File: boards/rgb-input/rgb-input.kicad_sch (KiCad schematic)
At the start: 22 parts, among them J1 Conn_01x03, J10 Conn_01x03, J11 Conn_01x03, J12 Conn_01x03, J15 Conn_01x03, J16 Conn_01x03, J17 Conn_01x03, J18 Conn_01x03, J2 Conn_01x03, J3 Conn_01x03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

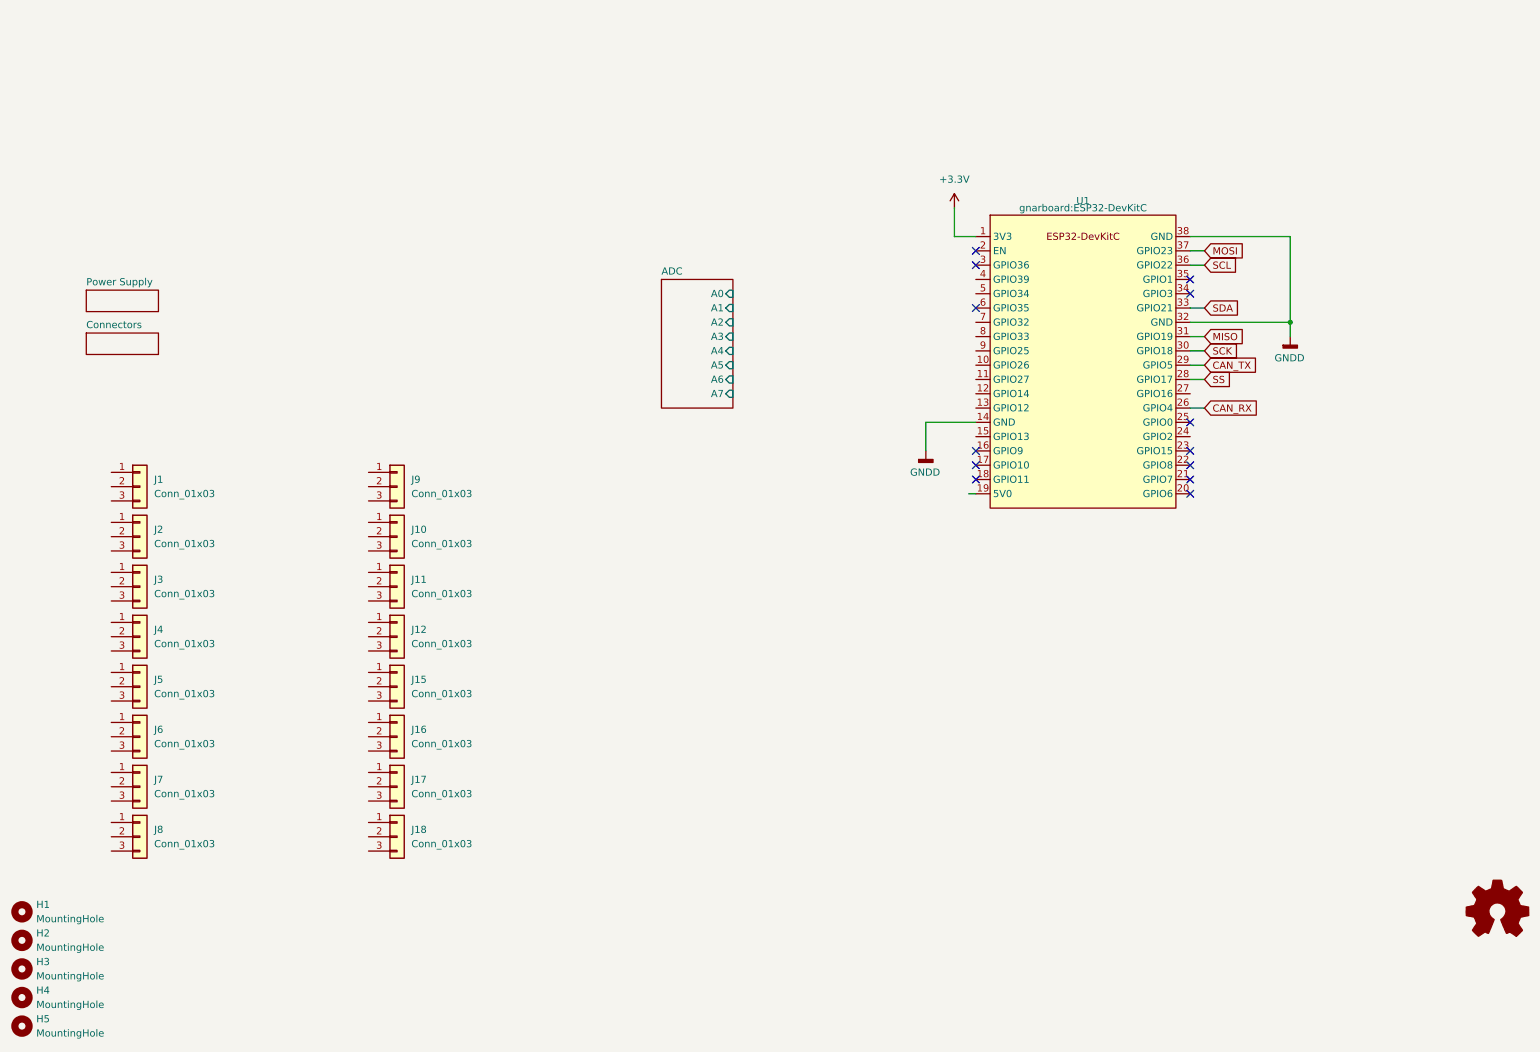
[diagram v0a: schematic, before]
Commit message: input board shaping up to be lit.
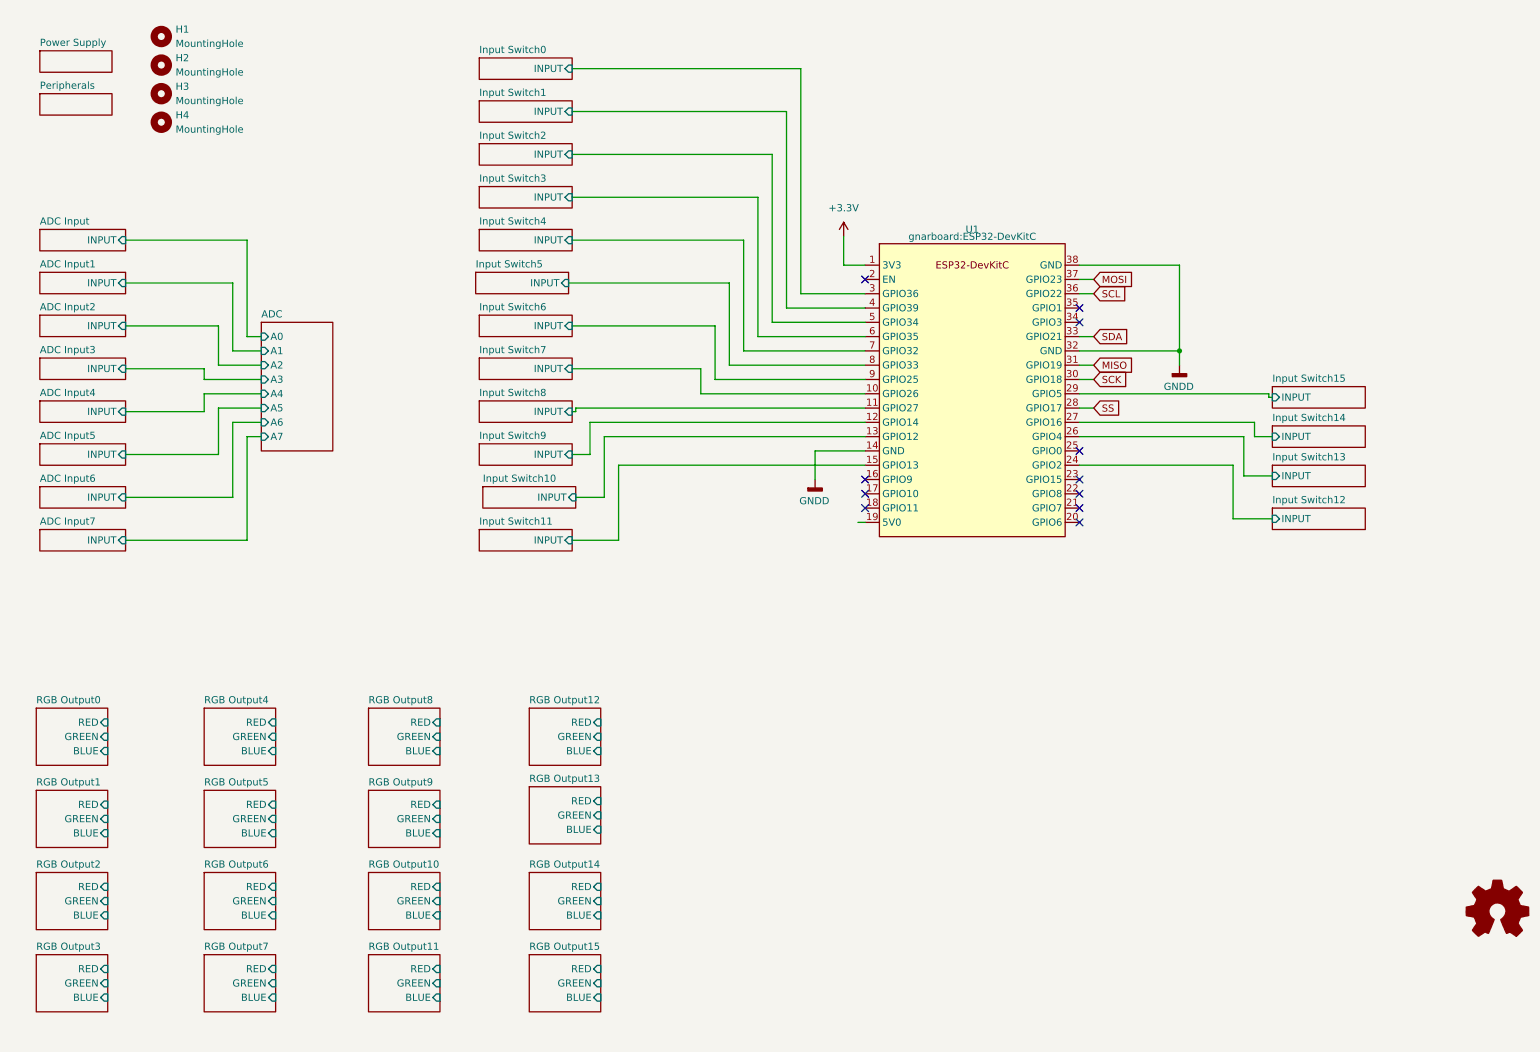
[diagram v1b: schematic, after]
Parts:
- removed H5: MountingHole, MountingHole:MountingHole_3.2mm_M3_DIN965_Pad, symbol Mechanical:MountingHole
- removed J1, J10, J11, J12, J15, J16, J17, J18, J2, J3, J4, J5, J6, J7, J8, J9: Conn_01x03, Connector_JST:JST_PH_B3B-PH-K_1x03_P2.00mm_Vertical, symbol Connector_Generic:Conn_01x03
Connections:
- net Input Switch7/INPUT: now reaches U1.10 (GPIO26)
- net Input Switch8/INPUT: now reaches U1.11 (GPIO27)
- net Input Switch9/INPUT: now reaches U1.12 (GPIO14)
- net Input Switch10/INPUT: now reaches U1.13 (GPIO12)
- net Input Switch11/INPUT: now reaches U1.15 (GPIO13)
- net Input Switch12/INPUT: now reaches U1.24 (GPIO2)
- net Input Switch14/INPUT: now reaches U1.27 (GPIO16)
- net Input Switch0/INPUT: now reaches U1.3 (GPIO36)
- net Input Switch1/INPUT: now reaches U1.4 (GPIO39)
- net Input Switch2/INPUT: now reaches U1.5 (GPIO34)
- net Input Switch3/INPUT: now reaches U1.6 (GPIO35)
- net Input Switch4/INPUT: now reaches U1.7 (GPIO32)
- net Input Switch5/INPUT: now reaches U1.8 (GPIO33)
- net Input Switch6/INPUT: now reaches U1.9 (GPIO25)
- net CAN_RX renamed Input Switch13/INPUT
- net CAN_TX renamed Input Switch15/INPUT
- no-connect marks 13 -> 11
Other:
- sheet Connectors renamed Peripherals
- added sheet ADC Input (adc input.kicad_sch)
- added sheet ADC Input1 (adc input.kicad_sch)
- added sheet ADC Input2 (adc input.kicad_sch)
- added sheet ADC Input3 (adc input.kicad_sch)
- added sheet ADC Input4 (adc input.kicad_sch)
- added sheet ADC Input5 (adc input.kicad_sch)
- added sheet ADC Input6 (adc input.kicad_sch)
- added sheet ADC Input7 (adc input.kicad_sch)
- added sheet Input Switch0 (input switch.kicad_sch)
- added sheet Input Switch1 (input switch.kicad_sch)
- added sheet Input Switch10 (input switch.kicad_sch)
- added sheet Input Switch11 (input switch.kicad_sch)
- added sheet Input Switch12 (input switch.kicad_sch)
- added sheet Input Switch13 (input switch.kicad_sch)
- added sheet Input Switch14 (input switch.kicad_sch)
- added sheet Input Switch15 (input switch.kicad_sch)
- added sheet Input Switch2 (input switch.kicad_sch)
- added sheet Input Switch3 (input switch.kicad_sch)
- added sheet Input Switch4 (input switch.kicad_sch)
- added sheet Input Switch5 (input switch.kicad_sch)
- added sheet Input Switch6 (input switch.kicad_sch)
- added sheet Input Switch7 (input switch.kicad_sch)
- added sheet Input Switch8 (input switch.kicad_sch)
- added sheet Input Switch9 (input switch.kicad_sch)
- added sheet RGB Output0 (rgb.kicad_sch)
- added sheet RGB Output1 (rgb.kicad_sch)
- added sheet RGB Output10 (rgb.kicad_sch)
- added sheet RGB Output11 (rgb.kicad_sch)
- added sheet RGB Output12 (rgb.kicad_sch)
- added sheet RGB Output13 (rgb.kicad_sch)
- added sheet RGB Output14 (rgb.kicad_sch)
- added sheet RGB Output15 (rgb.kicad_sch)
- added sheet RGB Output2 (rgb.kicad_sch)
- added sheet RGB Output3 (rgb.kicad_sch)
- added sheet RGB Output4 (rgb.kicad_sch)
- added sheet RGB Output5 (rgb.kicad_sch)
- added sheet RGB Output6 (rgb.kicad_sch)
- added sheet RGB Output7 (rgb.kicad_sch)
- added sheet RGB Output8 (rgb.kicad_sch)
- added sheet RGB Output9 (rgb.kicad_sch)
- sheet Peripherals: file connectors.kicad_sch -> peripherals.kicad_sch
- moved on the sheet: H1, H2, H3, H4, U1

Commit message: this board is going to be sick.
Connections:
- net ESP32_VIN: now reaches U1.19 (5V0)
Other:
- removed sheet RGB Output0
- removed sheet RGB Output1
- removed sheet RGB Output10
- removed sheet RGB Output11
- removed sheet RGB Output12
- removed sheet RGB Output13
- removed sheet RGB Output14
- removed sheet RGB Output15
- removed sheet RGB Output2
- removed sheet RGB Output3
- removed sheet RGB Output4
- removed sheet RGB Output5
- removed sheet RGB Output6
- removed sheet RGB Output7
- removed sheet RGB Output8
- removed sheet RGB Output9
- added sheet LEDS (leds.kicad_sch)
- moved on the sheet: H1, H2, H3, H4, U1

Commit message: figured out most of the components, working on placement
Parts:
- added J42: INPUTS, Connector_IDC:IDC-Header_2x10_P2.54mm_Vertical, symbol Connector_Generic:Conn_02x10_Odd_Even
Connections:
- net +3.3V: now also J42.1 (Pin_1), J42.3 (Pin_3)
- net GNDD: now also J42.2 (Pin_2), J42.4 (Pin_4)
- net Input Switch0/INPUT renamed INPUT0
- net INPUT0: now also J42.5 (Pin_5)
- net Input Switch1/INPUT renamed INPUT1
- net INPUT1: now also J42.6 (Pin_6)
- net Input Switch10/INPUT renamed INPUT10
- net INPUT10: now also J42.15 (Pin_15)
- net Input Switch11/INPUT renamed INPUT11
- net INPUT11: now also J42.16 (Pin_16)
- net Input Switch12/INPUT renamed INPUT12
- net INPUT12: now also J42.17 (Pin_17)
- net Input Switch13/INPUT renamed INPUT13
- net INPUT13: now also J42.18 (Pin_18)
- net Input Switch14/INPUT renamed INPUT14
- net INPUT14: now also J42.19 (Pin_19)
- net Input Switch15/INPUT renamed INPUT15
- net INPUT15: now also J42.20 (Pin_20)
- net Input Switch2/INPUT renamed INPUT2
- net INPUT2: now also J42.7 (Pin_7)
- net Input Switch3/INPUT renamed INPUT3
- net INPUT3: now also J42.8 (Pin_8)
- net Input Switch4/INPUT renamed INPUT4
- net INPUT4: now also J42.9 (Pin_9)
- net Input Switch5/INPUT renamed INPUT5
- net INPUT5: now also J42.10 (Pin_10)
- net Input Switch6/INPUT renamed INPUT6
- net INPUT6: now also J42.11 (Pin_11)
- net Input Switch7/INPUT renamed INPUT7
- net INPUT7: now also J42.12 (Pin_12)
- net Input Switch8/INPUT renamed INPUT8
- net INPUT8: now also J42.13 (Pin_13)
- net Input Switch9/INPUT renamed INPUT9
- net INPUT9: now also J42.14 (Pin_14)
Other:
- sheet ADC Input renamed ADC Input0

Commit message: too much routing
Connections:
- net INPUT0: now also U1.15 (GPIO13); no longer U1.3 (GPIO36)
- net INPUT1: now also U1.13 (GPIO12); no longer U1.4 (GPIO39)
- net INPUT10: now also U1.4 (GPIO39); no longer U1.13 (GPIO12)
- net INPUT11: now also U1.3 (GPIO36); no longer U1.15 (GPIO13)
- net INPUT2: now also U1.12 (GPIO14); no longer U1.5 (GPIO34)
- net INPUT3: now also U1.11 (GPIO27); no longer U1.6 (GPIO35)
- net INPUT4: now also U1.10 (GPIO26); no longer U1.7 (GPIO32)
- net INPUT5: now also U1.9 (GPIO25); no longer U1.8 (GPIO33)
- net INPUT6: now also U1.8 (GPIO33); no longer U1.9 (GPIO25)
- net INPUT7: now also U1.7 (GPIO32); no longer U1.10 (GPIO26)
- net INPUT8: now also U1.6 (GPIO35); no longer U1.11 (GPIO27)
- net INPUT9: now also U1.5 (GPIO34); no longer U1.12 (GPIO14)

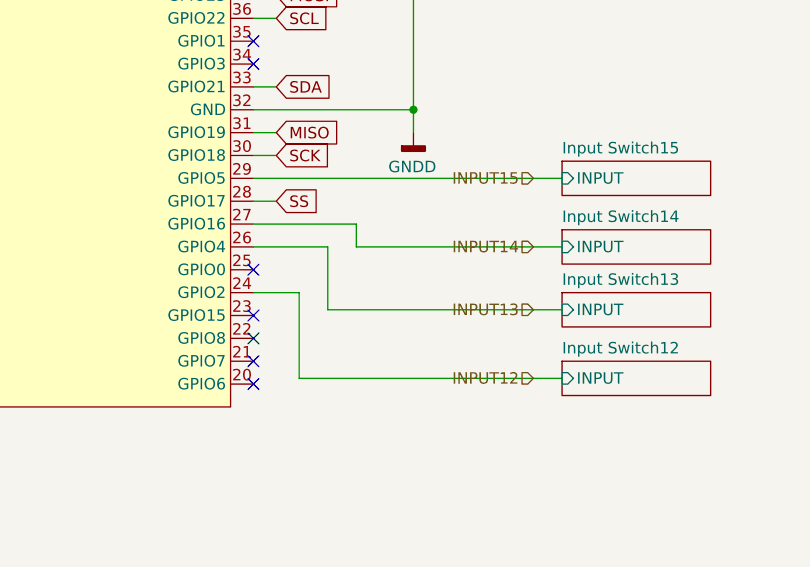
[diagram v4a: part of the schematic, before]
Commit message: whoa, board is fully routed!!!!
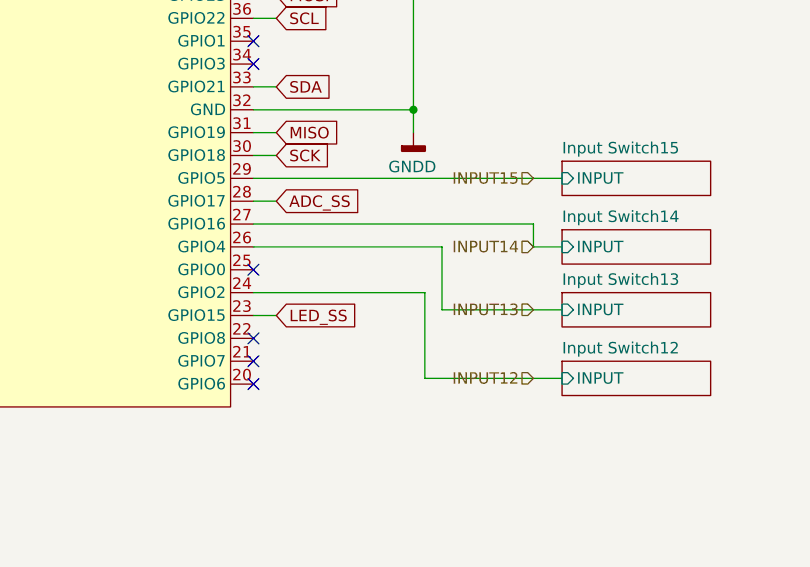
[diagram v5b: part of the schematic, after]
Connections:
- net LED_SS: now reaches U1.23 (GPIO15)
- net SS renamed ADC_SS
- no-connect marks 11 -> 10
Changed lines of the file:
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@@
   (junction (at 212.09 26.67) (diameter 0) (color 0 0 0 0)
   )
-  (no_connect (at 221.615 124.46))
   (no_connect (at 183.515 88.9))
   (no_connect (at 221.615 129.54))
@@
     (stroke (width 0) (type default))
   )
-  (wire (pts (xy 229.87 123.825) (xy 229.87 116.84))
+  (wire (pts (xy 242.57 123.825) (xy 242.57 116.84))
     (stroke (width 0) (type default))
   )
@@
     (stroke (width 0) (type default))
   )
+  (wire (pts (xy 221.615 124.46) (xy 224.155 124.46))
+    (stroke (width 0) (type default))
+  )
   (wire (pts (xy 161.29 101.6) (xy 161.29 81.28))
     (stroke (width 0) (type default))
@@
     (stroke (width 0) (type default))
   )
-  (wire (pts (xy 233.045 116.84) (xy 233.045 114.3))
+  (wire (pts (xy 252.73 116.84) (xy 252.73 114.3))
     (stroke (width 0) (type default))
   )
@@
     (stroke (width 0) (type default))
   )
-  (wire (pts (xy 226.695 121.92) (xy 221.615 121.92))
+  (wire (pts (xy 240.665 121.92) (xy 221.615 121.92))
     (stroke (width 0) (type default))
   )
@@
     (stroke (width 0) (type default))
   )
-  (wire (pts (xy 226.695 131.445) (xy 226.695 121.92))
+  (wire (pts (xy 240.665 131.445) (xy 240.665 121.92))
     (stroke (width 0) (type default))
   )
@@
     (stroke (width 0) (type default))
   )
-  (wire (pts (xy 229.87 116.84) (xy 221.615 116.84))
+  (wire (pts (xy 242.57 116.84) (xy 221.615 116.84))
     (stroke (width 0) (type default))
   )
@@
     (stroke (width 0) (type default))
   )
-  (wire (pts (xy 233.045 116.84) (xy 255.905 116.84))
+  (wire (pts (xy 252.73 116.84) (xy 255.905 116.84))
     (stroke (width 0) (type default))
   )
@@
     (stroke (width 0) (type default))
   )
-  (wire (pts (xy 229.87 123.825) (xy 255.905 123.825))
-    (stroke (width 0) (type default))
-  )
-  (wire (pts (xy 221.615 114.3) (xy 233.045 114.3))
+  (wire (pts (xy 242.57 123.825) (xy 255.905 123.825))
+    (stroke (width 0) (type default))
+  )
+  (wire (pts (xy 221.615 114.3) (xy 252.73 114.3))
     (stroke (width 0) (type default))
   )
@@
     (stroke (width 0) (type default))
   )
-  (wire (pts (xy 226.695 131.445) (xy 255.905 131.445))
+  (wire (pts (xy 240.665 131.445) (xy 255.905 131.445))
     (stroke (width 0) (type default))
   )
@@
     )
   )
-  (global_label "SS" (shape input) (at 224.155 111.76 0) (fields_autoplaced)
+  (global_label "ADC_SS" (shape input) (at 224.155 111.76 0) (fields_autoplaced)
     (effects (font (size 1.27 1.27)) (justify left))
-    (property "Intersheetrefs" "${INTERSHEET_REFS}" (at 229.5592 111.76 0)
+    (property "Intersheetrefs" "${INTERSHEET_REFS}" (at 234.1554 111.76 0)
       (effects (font (size 1.27 1.27)) (justify left) hide)
     )
+  )
+  (global_label "LED_SS" (shape input) (at 224.155 124.46 0) (fields_autoplaced)
+    (effects (font (size 1.27 1.27)) (justify left))
+    (property "Intersheetrefs" "${INTERSHEET_REFS}" (at 233.9739 124.46 0)
+      (effects (font (size 1.27 1.27)) (justify left) hide)
+    )

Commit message: various cleanups and tidying
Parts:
- H1, H2, H3, H4: symbol Mechanical:MountingHole -> Mechanical:MountingHole_Pad
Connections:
- no-connect marks 10 -> 14
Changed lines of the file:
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@@
   )
   (no_connect (at 183.515 88.9))
+  (no_connect (at 15.875 175.895))
   (no_connect (at 221.615 129.54))
+  (no_connect (at 15.875 182.88))
+  (no_connect (at 15.875 196.85))
   (no_connect (at 183.515 127))
   (no_connect (at 183.515 129.54))
+  (no_connect (at 15.875 189.865))
   (no_connect (at 183.515 124.46))
   (no_connect (at 221.615 96.52))
@@
     )
   )
-  (symbol (lib_id "Mechanical:MountingHole") (at 15.875 189.23 0) (unit 1)
+  (symbol (lib_id "Mechanical:MountingHole_Pad") (at 15.875 187.325 0) (unit 1)
     (in_bom yes) (on_board yes) (dnp no) (fields_autoplaced)
-    (property "Reference" "H3" (at 18.415 187.96 0)
-      (effects (font (size 1.27 1.27)) (justify left))
-    )
-    (property "Value" "MountingHole" (at 18.415 190.5 0)
-      (effects (font (size 1.27 1.27)) (justify left))
-    )
-    (property "Footprint" "MountingHole:MountingHole_3.2mm_M3_DIN965_Pad" (at 15.875 189.23 0)
-      (effects (font (size 1.27 1.27)) hide)
-    )
-    (property "Datasheet" "~" (at 15.875 189.23 0)
-      (effects (font (size 1.27 1.27)) hide)
-    )
+    (property "Reference" "H3" (at 18.415 186.055 0)
+      (effects (font (size 1.27 1.27)) (justify left))
+    )
+    (property "Value" "MountingHole" (at 18.415 188.595 0)
+      (effects (font (size 1.27 1.27)) (justify left))
+    )
+    (property "Footprint" "MountingHole:MountingHole_3.2mm_M3_DIN965_Pad" (at 15.875 187.325 0)
+      (effects (font (size 1.27 1.27)) hide)
+    )
+    (property "Datasheet" "~" (at 15.875 187.325 0)
+      (effects (font (size 1.27 1.27)) hide)
+    )
+    (pin "1")
     (instances
       (project "rgb-input"
@@
     )
   )
-  (symbol (lib_id "Mechanical:MountingHole") (at 15.875 184.15 0) (unit 1)
+  (symbol (lib_id "Mechanical:MountingHole_Pad") (at 15.875 180.34 0) (unit 1)
     (in_bom yes) (on_board yes) (dnp no) (fields_autoplaced)
-    (property "Reference" "H2" (at 18.415 182.88 0)
-      (effects (font (size 1.27 1.27)) (justify left))
-    )
-    (property "Value" "MountingHole" (at 18.415 185.42 0)
-      (effects (font (size 1.27 1.27)) (justify left))
-    )
-    (property "Footprint" "MountingHole:MountingHole_3.2mm_M3_DIN965_Pad" (at 15.875 184.15 0)
-      (effects (font (size 1.27 1.27)) hide)
-    )
-    (property "Datasheet" "~" (at 15.875 184.15 0)
-      (effects (font (size 1.27 1.27)) hide)
-    )
+    (property "Reference" "H2" (at 18.415 179.07 0)
+      (effects (font (size 1.27 1.27)) (justify left))
+    )
+    (property "Value" "MountingHole" (at 18.415 181.61 0)
+      (effects (font (size 1.27 1.27)) (justify left))
+    )
+    (property "Footprint" "MountingHole:MountingHole_3.2mm_M3_DIN965_Pad" (at 15.875 180.34 0)
+      (effects (font (size 1.27 1.27)) hide)
+    )
+    (property "Datasheet" "~" (at 15.875 180.34 0)
+      (effects (font (size 1.27 1.27)) hide)
+    )
+    (pin "1")
     (instances
       (project "rgb-input"
@@
     )
   )
-  (symbol (lib_id "Mechanical:MountingHole") (at 15.875 179.07 0) (unit 1)
+  (symbol (lib_id "Mechanical:MountingHole_Pad") (at 15.875 173.355 0) (unit 1)
     (in_bom yes) (on_board yes) (dnp no) (fields_autoplaced)
-    (property "Reference" "H1" (at 18.415 177.8 0)
-      (effects (font (size 1.27 1.27)) (justify left))
-    )
-    (property "Value" "MountingHole" (at 18.415 180.34 0)
-      (effects (font (size 1.27 1.27)) (justify left))
-    )
-    (property "Footprint" "MountingHole:MountingHole_3.2mm_M3_DIN965_Pad" (at 15.875 179.07 0)
-      (effects (font (size 1.27 1.27)) hide)
-    )
-    (property "Datasheet" "~" (at 15.875 179.07 0)
-      (effects (font (size 1.27 1.27)) hide)
-    )
+    (property "Reference" "H1" (at 18.415 172.085 0)
+      (effects (font (size 1.27 1.27)) (justify left))
+    )
+    (property "Value" "MountingHole" (at 18.415 174.625 0)
+      (effects (font (size 1.27 1.27)) (justify left))
+    )
+    (property "Footprint" "MountingHole:MountingHole_3.2mm_M3_DIN965_Pad" (at 15.875 173.355 0)
+      (effects (font (size 1.27 1.27)) hide)
+    )
+    (property "Datasheet" "~" (at 15.875 173.355 0)
+      (effects (font (size 1.27 1.27)) hide)
+    )
+    (pin "1")
     (instances
       (project "rgb-input"
@@
     )
   )
-  (symbol (lib_id "Mechanical:MountingHole") (at 15.875 194.31 0) (unit 1)
+  (symbol (lib_id "Mechanical:MountingHole_Pad") (at 15.875 194.31 0) (unit 1)
     (in_bom yes) (on_board yes) (dnp no) (fields_autoplaced)
     (property "Reference" "H4" (at 18.415 193.04 0)
@@
       (effects (font (size 1.27 1.27)) hide)
     )
-    (instances
-      (project "rgb-input"
+    (pin "1")
+    (instances
+      (project "rgb-input"
